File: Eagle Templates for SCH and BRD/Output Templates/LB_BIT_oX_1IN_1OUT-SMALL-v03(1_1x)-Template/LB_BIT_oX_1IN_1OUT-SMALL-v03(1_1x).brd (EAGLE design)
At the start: 21.4 x 11.6 mm, 17 parts, among them U1 LV321SOT23-5, U2 LV321SOT23-5

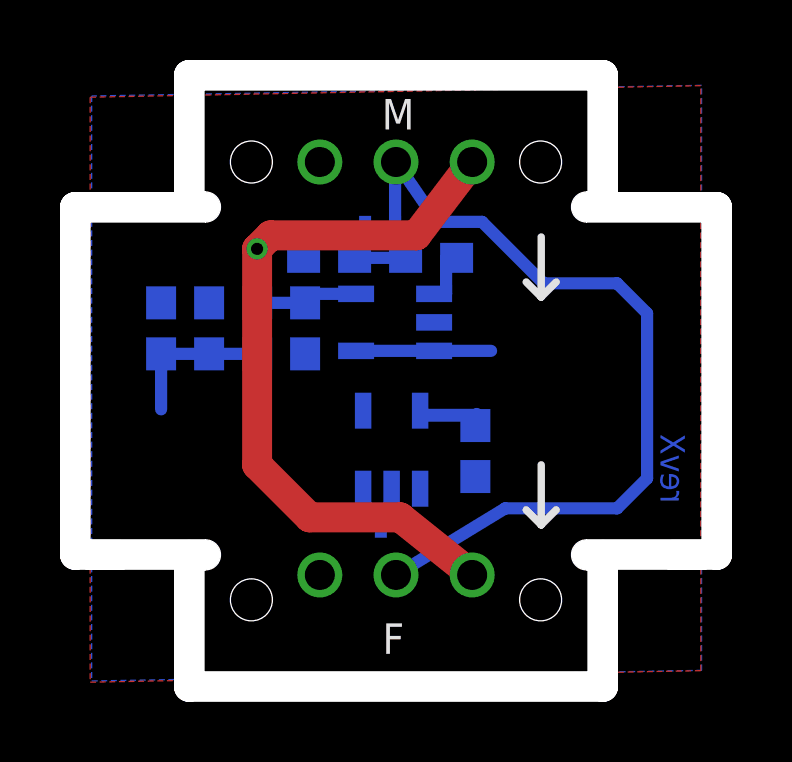
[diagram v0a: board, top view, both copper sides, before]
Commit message: added bitlab logo and made minor changes to board templates. Updated littlebits library.
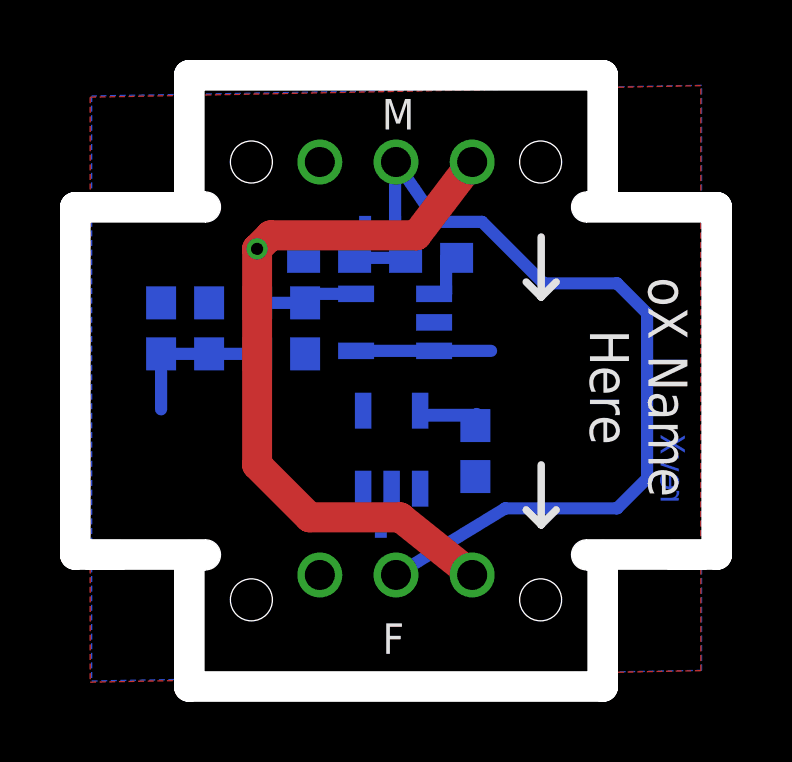
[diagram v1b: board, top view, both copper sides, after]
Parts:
- added U$5: (no value), LITTLEBITS:BITLAB-LOGO
- moved U$4 3.51 mm to (15.4, 9.90)
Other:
- board text added: "oX Name Here"
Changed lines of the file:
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@@
 <layer number="111" name="LB_TEXT" color="13" fill="1" visible="yes" active="yes"/>
 <layer number="112" name="tSilk" color="7" fill="1" visible="yes" active="yes"/>
+<layer number="113" name="ReferenceLS" color="7" fill="1" visible="no" active="yes"/>
 <layer number="116" name="Patch_BOT" color="9" fill="4" visible="yes" active="yes"/>
+<layer number="118" name="Rect_Pads" color="7" fill="1" visible="no" active="yes"/>
 <layer number="121" name="_tsilk" color="7" fill="1" visible="yes" active="yes"/>
 <layer number="122" name="_bsilk" color="7" fill="1" visible="yes" active="yes"/>
@@
 <wire x1="23.91" y1="15.705" x2="23.91" y2="4.11" width="1" layer="46"/>
 <wire x1="22.41" y1="15.705" x2="23.91" y2="15.705" width="1" layer="46"/>
+<text x="21.3" y="9.7" size="1.3" layer="21" font="vector" rot="SR270" align="center">oX Name
+Here</text>
 </plain>
 <attributes>
@@
 <element name="U$2" library="LITTLEBITS131206" package="OSHW-LOGO-L" value="OSHW-LOGOL" x="-33.025" y="-66.05"/>
 <element name="U$1" library="LITTLEBITS" package="OSHWCREDIT" value="OSHWCREDIT" x="-93.47" y="-62.25"/>
-<element name="U$4" library="ohw-logo" package="OSHW_FILLX150_NOTEXT" value="" x="18.9" y="10.2" rot="MR90"/>
+<element name="U$4" library="ohw-logo" package="OSHW_FILLX150_NOTEXT" value="" x="15.4" y="9.9" rot="MR90"/>
 <element name="U$3" library="LITTLEBITS" package="FABDWG01-OHW" value="FRAME-LETTER" x="0" y="0"/>
+<element name="U$5" library="LITTLEBITS" package="BITLAB-LOGO" value="" x="19.8" y="14.1" rot="R270"/>
 </elements>
 <signals>

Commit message: Updated templates
- Added ferrite beads
- Moved text and annotations off of Nets layer
- Minor layout changes
- Removed I/O/W prefix from reference designators
- Removed output stage components from output bits
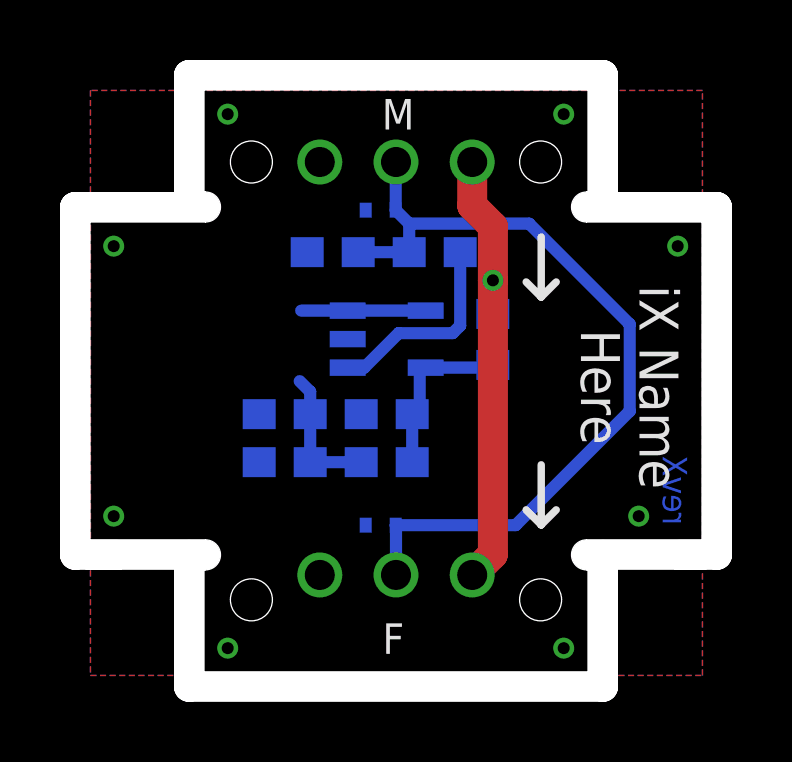
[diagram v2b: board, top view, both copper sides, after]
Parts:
- removed I?C1: 0.1uF, LITTLEBITS:CAP-0603
- removed I?C2: 10uF, LITTLEBITS:CAP-0603
- removed I?C3: 1.0uF, LITTLEBITS:CAP-0603
- removed I?R1: 1meg, LITTLEBITS:RES-0603
- removed I?R2: 10K, LITTLEBITS:RES-0603
- removed I?R3, I?R4: 3K3, LITTLEBITS:RES-0603
- removed I?TVS1, I?TVS2: ESD9B5.0ST5G, LITTLEBITS:SOD-923
- removed U2: LV321SOT23-5, LITTLEBITS:SOT23-5
- added C1: 0.1uF, LITTLEBITS:CAP-0603
- added C2: 10uF, LITTLEBITS:CAP-0603
- added FB1: FERRITE-BEAD0603, LITTLEBITS:R0603
- added R1: 1meg, LITTLEBITS:RES-0603
- added R2: 10K, LITTLEBITS:RES-0603
- added R3, R4: 3K3, LITTLEBITS:RES-0603
- added TVS1, TVS2: ESD9B5.0ST5G, LITTLEBITS:SOD-923
- U$1: value OSHWCREDIT -> OSHW-LOGOL; device LITTLEBITS:OSHWCREDIT -> LITTLEBITS131206:OSHW-LOGO-L
- U$2: value OSHW-LOGOL -> OSHWCREDIT; device LITTLEBITS131206:OSHW-LOGO-L -> LITTLEBITS:OSHWCREDIT
- moved U$2 59.2 mm to (-92.2, -64.3)
- moved U$1 56.3 mm to (-37.5, -68.2)
- moved U1 0.63 mm to (12.9, 11.3), turned to 90 degrees
- moved U$5 0.10 mm to (19.8, 14.0)
- renumbered I?BSF to BSF1, I?BSM to BSM1
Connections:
- removed net N$3: U2.1
- removed net SIG_IN: BSF1.SIG, BSM1.SIG1, I?R1.2, I?R2.2, I?TVS1.2
- removed net SIG_OUT: I?TVS2.2, U2.3, U2.4
- new net LB_VCC: BSF1.VCC, BSM1.VCC1, FB1.2
- new net SIG: BSF1.SIG, BSM1.SIG1, R1.2, R2.2, TVS1.2, TVS2.2
- net GND: now also C1.2, C2.2, R1.1, R4.1, TVS1.1, TVS2.1; no longer I?C1.2, I?C2.2, I?C3.1, I?R1.1, I?R4.1, I?TVS1.1, I?TVS2.1, U2.2
- net N$4: now also R2.1; no longer I?R2.1
- net VCC: now also C1.1, FB1.1, R3.2; no longer BSF1.VCC, BSM1.VCC1, I?C1.1, I?C3.2, I?R3.2, U2.5
- net VREF: now also C2.1, R3.1, R4.2; no longer I?C2.1, I?R3.1, I?R4.2
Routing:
- net SIG_IN: track 30.8 -> 0.00 mm
- net SIG: track 0.00 -> 27.6 mm
- net VCC: track 29.7 -> 5.91 mm, vias 1 -> 0
- net LB_VCC: track 0.00 -> 15.5 mm, vias 0 -> 1
- net N$4: track 1.95 -> 6.78 mm
- net S$1: track 3.78 -> 0.00 mm
- net VREF: track 5.10 -> 4.54 mm
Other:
- outline, holes or cut-outs redrawn
- board text added: "iX Name Here"
- board text removed: "oX Name Here"
